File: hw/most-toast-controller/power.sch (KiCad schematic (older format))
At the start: 4 parts, among them U2 MIC5353

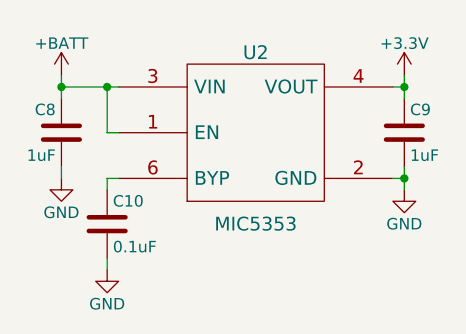
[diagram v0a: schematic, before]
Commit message: started putting most-toast on a board. Turns out one inch makes for very very small PCB
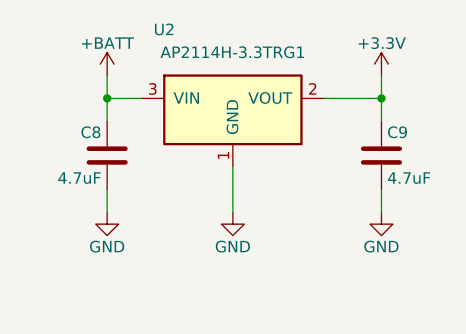
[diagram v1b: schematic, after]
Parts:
- removed C10: 0.1uF, symbol C
- removed U2: MIC5353, symbol MIC5353
- added U2: AP2114H-3.3TRG1, TO_SOT_Packages_SMD:SOT-223, symbol AP2114H-3.3TRG1
- C8, C9: value 1uF -> 4.7uF; footprint (none) -> Capacitors_SMD:C_0805_HandSoldering
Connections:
- net +3V3: now also U2.2 (VOUT)
- net +BATT: now also U2.3 (VIN)
- net GND: now also U2.1 (GND)
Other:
- moved on the sheet: C8, C9
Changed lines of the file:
@@
 EESchema Schematic File Version 2
+LIBS:regul
 LIBS:power
 LIBS:device
@@
 LIBS:conn
 LIBS:linear
-LIBS:regul
 LIBS:74xx
 LIBS:cmos4000
@@
 $EndDescr
 $Comp
-L MIC5353 U2
-U 1 1 564DFE82
-P 5050 3250
-F 0 "U2" H 5050 3700 60  0000 C CNN
-F 1 "MIC5353" H 5050 2950 60  0000 C CNN
-F 2 "" H 5050 3250 60  0000 C CNN
-F 3 "" H 5050 3250 60  0000 C CNN
-	1    5050 3250
-	1    0    0    -1
-$EndComp
-$Comp
 L C C9
 U 1 1 564DFFBA
-P 5700 3150
-F 0 "C9" H 5725 3250 50  0000 L CNN
-F 1 "1uF" H 5725 3050 50  0000 L CNN
-F 2 "" H 5738 3000 30  0000 C CNN
-F 3 "" H 5700 3150 60  0000 C CNN
-	1    5700 3150
+P 5600 3250
+F 0 "C9" H 5625 3350 50  0000 L CNN
+F 1 "4.7uF" H 5625 3150 50  0000 L CNN
+F 2 "Capacitors_SMD:C_0805_HandSoldering" H 5638 3100 30  0001 C CNN
+F 3 "" H 5600 3250 60  0000 C CNN
+	1    5600 3250
 	1    0    0    -1
 $EndComp
@@
 L C C8
 U 1 1 564E0063
-P 4200 3150
-F 0 "C8" H 4225 3250 50  0000 L CNN
-F 1 "1uF" H 4225 3050 50  0000 L CNN
-F 2 "" H 4238 3000 30  0000 C CNN
-F 3 "" H 4200 3150 60  0000 C CNN
-	1    4200 3150
+P 4400 3250
+F 0 "C8" H 4425 3350 50  0000 L CNN
+F 1 "4.7uF" H 4425 3150 50  0000 L CNN
+F 2 "Capacitors_SMD:C_0805_HandSoldering" H 4438 3100 30  0001 C CNN
+F 3 "" H 4400 3250 60  0000 C CNN
+	1    4400 3250
 	-1   0    0    -1
 $EndComp
+Wire Wire Line
+	5600 2900 5600 3100
+Wire Wire Line
+	5600 3400 5600 3500
 $Comp
-L C C10
-U 1 1 564E0086
-P 4400 3550
-F 0 "C10" H 4425 3650 50  0000 L CNN
-F 1 "0.1uF" H 4425 3450 50  0000 L CNN
-F 2 "" H 4438 3400 30  0000 C CNN
-F 3 "" H 4400 3550 60  0000 C CNN
-	1    4400 3550
+L GND #PWR018
+U 1 1 564E040A
+P 5600 3500
+F 0 "#PWR018" H 5600 3250 50  0001 C CNN
+F 1 "GND" H 5600 3350 50  0000 C CNN
+F 2 "" H 5600 3500 60  0000 C CNN
+F 3 "" H 5600 3500 60  0000 C CNN
+	1    5600 3500
+	1    0    0    -1
+$EndComp
+$Comp
+L GND #PWR019
+U 1 1 564E05F7
+P 4400 3500
+F 0 "#PWR019" H 4400 3250 50  0001 C CNN
+F 1 "GND" H 4400 3350 50  0000 C CNN
+F 2 "" H 4400 3500 60  0000 C CNN
+F 3 "" H 4400 3500 60  0000 C CNN
+	1    4400 3500
 	1    0    0    -1
 $EndComp
 Wire Wire Line
-	4450 3350 4400 3350
-Wire Wire Line
-	4400 3350 4400 3400
+	4400 3400 4400 3500
 $Comp
-L GND #PWR22
-U 1 1 564E0146
-P 4400 3750
-F 0 "#PWR22" H 4400 3500 50  0001 C CNN
-F 1 "GND" H 4400 3600 50  0000 C CNN
-F 2 "" H 4400 3750 60  0000 C CNN
-F 3 "" H 4400 3750 60  0000 C CNN
-	1    4400 3750
+L +3.3V #PWR020
+U 1 1 564E0785
+P 5600 2900
+F 0 "#PWR020" H 5600 2750 50  0001 C CNN
+F 1 "+3.3V" H 5600 3040 50  0000 C CNN
+F 2 "" H 5600 2900 60  0000 C CNN
+F 3 "" H 5600 2900 60  0000 C CNN
+	1    5600 2900
+	1    0    0    -1
+$EndComp
+$Comp
+L +BATT #PWR021
+U 1 1 564E0871
+P 4400 2900
+F 0 "#PWR021" H 4400 2750 50  0001 C CNN
+F 1 "+BATT" H 4400 3040 50  0000 C CNN
+F 2 "" H 4400 2900 60  0000 C CNN
+F 3 "" H 4400 2900 60  0000 C CNN
+	1    4400 2900
+	1    0    0    -1
+$EndComp
+$Comp
+L AP2114H-3.3TRG1 U2
+U 1 1 5653FBCC
+P 4950 3000
+F 0 "U2" H 4650 3300 50  0000 C CNN
+F 1 "AP2114H-3.3TRG1" H 4950 3200 50  0000 C CNN
+F 2 "TO_SOT_Packages_SMD:SOT-223" H 5150 2700 50  0001 C CIN
+F 3 "" H 4950 3000 60  0000 C CNN
+	1    4950 3000
 	1    0    0    -1
 $EndComp
 Wire Wire Line
-	4400 3700 4400 3750
-Wire Wire Line
-	5650 2950 5700 2950
-Wire Wire Line
-	5700 2900 5700 3000
-Wire Wire Line
-	5650 3350 5700 3350
-Wire Wire Line
-	5700 3300 5700 3400
-Wire Wire Line
-	4450 3150 4400 3150
-Wire Wire Line
-	4400 3150 4400 2950
-Wire Wire Line
-	4200 2950 4450 2950
+	5350 3000 5600 3000
+Connection ~ 5600 3000
 $Comp
-L GND #PWR21
-U 1 1 564E040A
-P 5700 3400
-F 0 "#PWR21" H 5700 3150 50  0001 C CNN
-F 1 "GND" H 5700 3250 50  0000 C CNN
-F 2 "" H 5700 3400 60  0000 C CNN
-F 3 "" H 5700 3400 60  0000 C CNN
-	1    5700 3400
-	1    0    0    -1
-$EndComp
-Connection ~ 5700 3350
-$Comp
-L GND #PWR20
-U 1 1 564E05F7
-P 4200 3350
-F 0 "#PWR20" H 4200 3100 50  0001 C CNN
-F 1 "GND" H 4200 3200 50  0000 C CNN
-F 2 "" H 4200 3350 60  0000 C CNN
-F 3 "" H 4200 3350 60  0000 C CNN
-	1    4200 3350
+L GND #PWR022
+U 1 1 565400AD
+P 4950 3500
+F 0 "#PWR022" H 4950 3250 50  0001 C CNN
+F 1 "GND" H 4950 3350 50  0000 C CNN
+F 2 "" H 4950 3500 60  0000 C CNN
+F 3 "" H 4950 3500 60  0000 C CNN
+	1    4950 3500
 	1    0    0    -1
 $EndComp
 Wire Wire Line
-	4200 3300 4200 3350
-Connection ~ 4400 2950
+	4950 3300 4950 3500
 Wire Wire Line
-	4200 2900 4200 3000
-$Comp
-L +3.3V #PWR19
-U 1 1 564E0785
-P 5700 2900
-F 0 "#PWR19" H 5700 2750 50  0001 C CNN
-F 1 "+3.3V" H 5700 3040 50  0000 C CNN
-F 2 "" H 5700 2900 60  0000 C CNN
-F 3 "" H 5700 2900 60  0000 C CNN
-	1    5700 2900
-	1    0    0    -1
-$EndComp
-Connection ~ 5700 2950
-$Comp
-L +BATT #PWR18
-U 1 1 564E0871
-P 4200 2900
-F 0 "#PWR18" H 4200 2750 50  0001 C CNN
-F 1 "+BATT" H 4200 3040 50  0000 C CNN
-F 2 "" H 4200 2900 60  0000 C CNN
-F 3 "" H 4200 2900 60  0000 C CNN
-	1    4200 2900
-	1    0    0    -1
-$EndComp
-Connection ~ 4200 2950
+	4400 3100 4400 2900
+Wire Wire Line
+	4550 3000 4400 3000
+Connection ~ 4400 3000
 $EndSCHEMATC
